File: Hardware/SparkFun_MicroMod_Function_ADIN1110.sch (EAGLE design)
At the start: 72 parts, among them J11 MICROMOD_STANDARD, Q1 220mA/50V/3.5Ω, Q5 20V/4.2A/52mΩ/1.4W, U1 EEPROM, U2 ADIN1110, U4 3.3V, Y1 25MHz

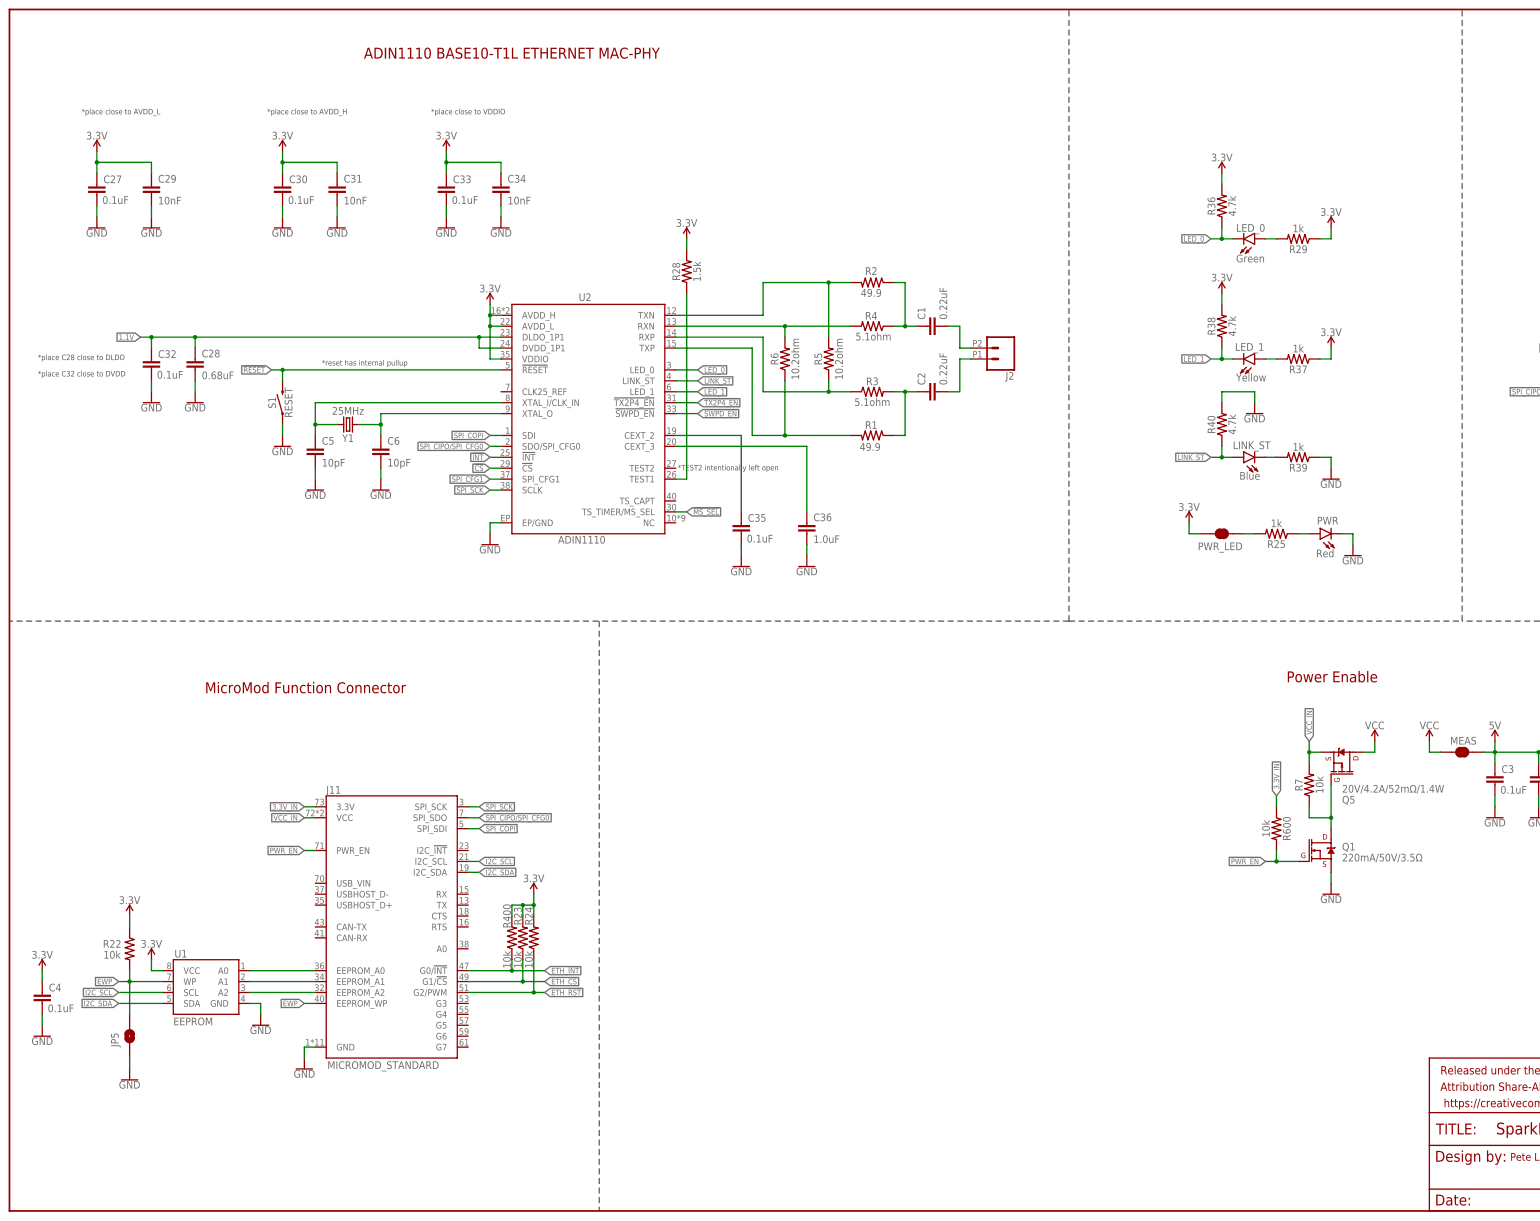
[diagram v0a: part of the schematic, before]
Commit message: HARTING T1 connector added and layout work
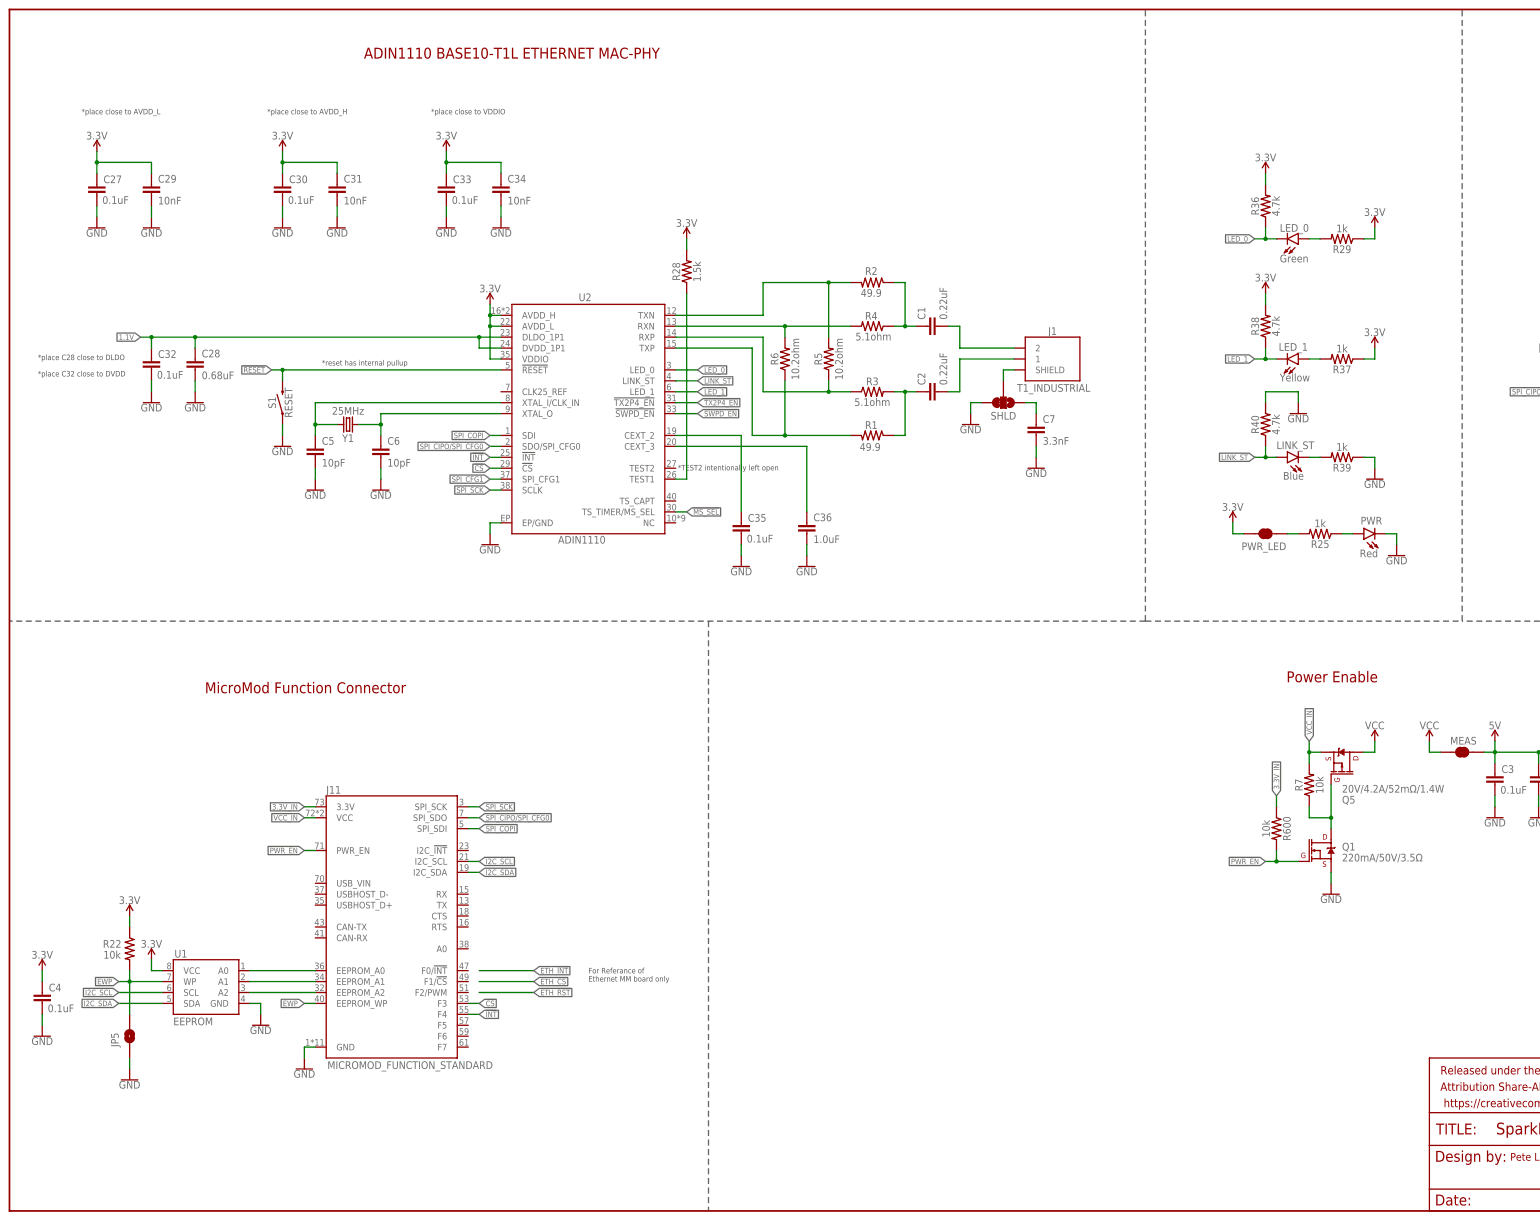
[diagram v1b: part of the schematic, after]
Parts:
- removed J2: (no value), SparkFun-Connectors:CONN_02SCREWTERMINAL-6.35MM-2
- removed R23, R24, R400: 10k, SparkFun-Resistors:10KOHM-0603-1/10W-1%
- added C7: 3.3nF, SparkFun-Capacitors:3.3NF-0603-100V-10%
- added J1: T1_INDUSTRIAL, ADIN1110:T1_INDUSTRIAL_JACK_AH_IP20
- added SHLD: JUMPER-SMT_3_1-NC_TRACE_SILK, SparkFun-Jumpers:JUMPER-SMT_3_1-NC_TRACE_SILK
- J11: value MICROMOD_STANDARD -> MICROMOD_FUNCTION_STANDARD; device SparkFun-MicroMod-Function:MICROMOD_STANDARD -> SparkFun-MicroMod:MICROMOD_FUNCTION_STANDARD
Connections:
- removed net ETH_!CS!: J11.G1/!CS!, R23.1
- removed net ETH_!INT!: J11.G0/!INT!, R400.1
- removed net ETH_!RST!: J11.G2/PWM, R24.1
- new net N$41: C7.1, SHLD.1
- new net N$43: J1.SHIELD, SHLD.2
- net !CS!: now also J11.F3
- net !INT!: now also J11.F4
- net 3.3V: no longer R23.2, R24.2, R400.2
- net GND: now also C7.2, SHLD.3
- net N$32: now also J1.2; no longer J2.1
- net N$34: now also J1.1; no longer J2.2
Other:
- note added: "For Referance of Ethernet MM board only"
- moved on the sheet: LED_0, LED_1, LINK_ST, PWR, PWR_LED, R25, R29, R36, R37, R38, R39, R40

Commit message: sch cleanup
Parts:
- added LOGO1: SFE_LOGO_NAME_FLAME.2_INCH, SparkFun-Aesthetics:SFE_LOGO_NAME_FLAME.2_INCH
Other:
- note added: "* For Referance of Ethernet MM board only"
- note added: "Configuration Pins/Jumpers"
- note added: "ETH_!CS!"
- note added: "ETH_!INT!"
- note added: "ETH_!RST!"
- note added: "STATUS LEDS"
- note removed: "For Referance of Ethernet MM board only"
- moved on the sheet: C13, C24, C3, C4, J11, JP5, MEAS, Q1, Q5, R22, R600, R7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

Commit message: some checklist catches - sch cleanup
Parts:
- removed C27, C30, C33: 0.1uF, SparkFun-Capacitors:0.1UF-0402T-16V-10%
- removed C29, C31, C34: 10nF, SparkFun-Capacitors:10NF-0402T-25V-10%
- removed Q5: 20V/4.2A/52mΩ/1.4W, SparkFun-DiscreteSemi:MOSFET_PCH-DMG2305UX-7
- removed R600: 10k, SparkFun-Resistors:10KOHM-0603-1/10W-1%
- added C10, C16: 0.1uF, SparkFun-Capacitors:0.1UF-0402T-16V-10%
- added C12, C14, C17: 10nF, SparkFun-Capacitors:10NF-0402T-25V-10%
- added C8: 1.0uF, SparkFun-Capacitors:1.0UF-0603-16V-10%
- added Q2: 20V/4.2A/52mΩ/1.4W, SparkFun-DiscreteSemi:MOSFET_PCH-DMG2305UX-7
- added R8: 10k, SparkFun-Resistors:10KOHM-0603-1/10W-1%
- C13: value 1.0uF -> 0.1uF; device SparkFun-Capacitors:1.0UF-0603-16V-10% -> SparkFun-Capacitors:0.1UF-0402T-16V-10%
- U1: value EEPROM -> ADIN1110; device SparkFun-IC-Memory:EEPROM-I2C512K -> ADIN1110:ADIN1110
- U2: value ADIN1110 -> EEPROM; device ADIN1110:ADIN1110 -> SparkFun-IC-Memory:EEPROM-I2C512K
- renumbered C24 to C9, C28 to C11, C32 to C15, C35 to C18, C36 to C19, J11 to J2, JP5 to EWP, R25 to R9, R28 to R10, R29 to R11, R31 to R12, R32 to R13, R33 to R14, R34 to R15, R35 to R16, R36 to R17, R37 to R20, R38 to R18, R39 to R21, R40 to R19, U4 to U3
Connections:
- removed net 5V: C13.1, C3.1, MEAS.2, U3.IN
- removed net VCC: MEAS.1, Q5.D
- new net N$1: MEAS.1, Q2.D
- new net N$2: C3.1, C8.1, MEAS.2, U3.IN
- net !CS!: now also U1.!CS!; no longer U2.!CS!
- net !INT!: now also U1.!INT!; no longer U2.!INT!
- net !MS_SEL!: now also U1.TS_TIMER/MS_SEL; no longer U2.TS_TIMER/MS_SEL
- net !RESET!: now also U1.!RESET!; no longer U2.!RESET!
- net !SWPD_EN!: now also U1.!SWPD_EN!; no longer U2.!SWPD_EN!
- net !TX2P4_EN!: now also U1.!TX2P4_EN!; no longer U2.!TX2P4_EN!
- net 1.1V: now also U1.DLDO_1P1, U1.DVDD_1P1; no longer U2.DLDO_1P1, U2.DVDD_1P1
- net 3.3V: now also C10.1, C12.1, C13.1, C14.1, C16.1, C17.1, R8.1, U1.AVDD_H, U1.AVDD_L, U1.VDDIO, U2.VCC; no longer C27.1, C29.1, C30.1, C31.1, C33.1, C34.1, R22.1, U1.VCC, U2.AVDD_H, U2.AVDD_L, U2.VDDIO
- net 3.3V_IN: now also R22.1; no longer R600.1
- net A0: now also U2.A0; no longer U1.A0
- net A1: now also U2.A1; no longer U1.A1
- net A2: now also U2.A2; no longer U1.A2
- net EWP: now also R8.2, U2.WP; no longer R22.2, U1.WP
- net GND: now also C10.2, C12.2, C14.2, C16.2, C17.2, C8.2, U1.EP/GND, U2.GND; no longer C27.2, C29.2, C30.2, C31.2, C33.2, C34.2, U1.GND, U2.EP/GND
- net I2C_SCL: now also U2.SCL; no longer U1.SCL
- net I2C_SDA: now also U2.SDA; no longer U1.SDA
- net LED_0: now also U1.LED_0; no longer U2.LED_0
- net LED_1: now also U1.LED_1; no longer U2.LED_1
- net LINK_ST: now also U1.LINK_ST; no longer U2.LINK_ST
- net N$11: now also Q2.G; no longer Q5.G
- net N$12: now also U1.XTAL_I/CLK_IN; no longer U2.XTAL_I/CLK_IN
- net N$14: now also U1.XTAL_O; no longer U2.XTAL_O
- net N$18: now also U1.TEST1; no longer U2.TEST1
- net N$21: now also U1.CEXT_2; no longer U2.CEXT_2
- net N$22: now also U1.CEXT_3; no longer U2.CEXT_3
- net N$35: now also U1.RXN; no longer U2.RXN
- net N$36: now also U1.RXP; no longer U2.RXP
- net N$37: now also U1.TXP; no longer U2.TXP
- net N$38: now also U1.TXN; no longer U2.TXN
- net PWR_EN: now also R22.2; no longer R600.2
- net SPI_CFG1: now also U1.SPI_CFG1; no longer U2.SPI_CFG1
- net SPI_CIPO/SPI_CFG0: now also U1.SDO/SPI_CFG0; no longer U2.SDO/SPI_CFG0
- net SPI_COPI: now also U1.SDI; no longer U2.SDI
- net SPI_SCK: now also U1.SCLK; no longer U2.SCLK
- net VCC_IN: now also Q2.S; no longer Q5.S
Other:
- note added: "*All hardare config pins default low with internal pull down resistors See datasheet page 16 for all available options."
- note added: "Connector Shield Grounding options Set jumper to select either direct connection, or through a cap."
- note added: "Cut Jumper to disable power LED"
- note added: "EEPROM Write Protect Open (default, HIGH): read & write allowed Closed (LOW): read allowed, write prohibited"
- note added: "VDD Ranges 3.13V - 3.46V [2.4V p-p or 1.0V p-p transmit level] 1.71V - 3.46V [1.0V p-p transmit level]"
- note removed: "*All hardare config pins default low with internal pull down resistors"
- moved on the sheet: C13, Q1, R22, R7

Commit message: Added transformer isolation and TVS diode array
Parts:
- added C20: 1.0nF (2kV), SparkFun-Capacitors:1.0NF/1000PF-1206-2KV-10%-X7R-WORTH-ELEKRONIK
- added C21: 0.1uF (50V), SparkFun-Capacitors:0.1UF-0402T-50V-10%-X7R-WE
- added C22: 0.1uF (100V), SparkFun-Capacitors:0.1UF-0603-100V-10%-X7R-WE
- added R23: 100, SparkFun-Resistors:100OHM-0603-1/10W-1%
- added T1: WE-STST, ADIN1110:WE_STST_TRANSFORMER_1:1_SMD_74930030_3.2X4.7MM
- added U4: WE-TVS, ADIN1110:WE-TVS_DIODE_ARRAY_824012823_1.0X1.2MM
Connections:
- new net N$3: C21.1, T1.5
- new net N$4: C22.1, T1.4
- new net N$5: J1.2, T1.6
- new net N$6: J1.1, T1.7
- new net N$7: C22.2, R23.1, T1.3
- new net N$8: C20.1, R23.2
- net GND: now also C20.2, C21.2, U4.3
- net N$32: now also T1.1, U4.2; no longer J1.2
- net N$34: now also T1.2, U4.1; no longer J1.1
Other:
- note added: "47-ETH_!INT!"
- note added: "49-ETH_!CS!"
- note added: "51-ETH_!RST!"
- note removed: "ETH_!CS!"
- note removed: "ETH_!INT!"
- note removed: "ETH_!RST!"
- moved on the sheet: C1, C11, C15, C18, C19, C2, C3, C5, C6, C7, C8, C9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
